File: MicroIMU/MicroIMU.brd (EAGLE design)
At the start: 8.1 x 9.3 mm, 17 parts

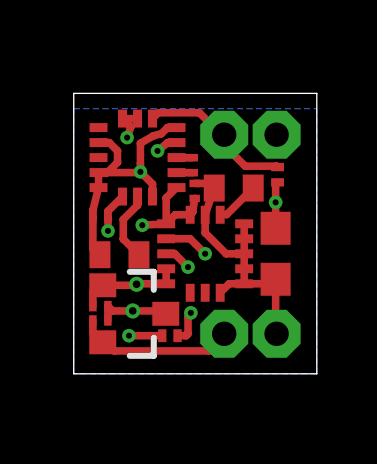
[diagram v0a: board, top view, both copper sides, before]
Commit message: changed to invense MPU9250
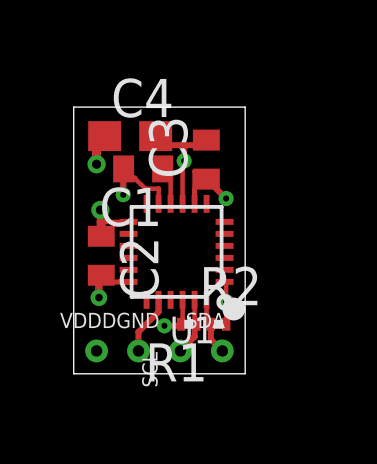
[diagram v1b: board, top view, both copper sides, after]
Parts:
- removed C5: 10uF, resistor:C0603
- removed C7: 0.01 uF, resistor:C0402
- removed C8: 4.7uF, resistor:C0402
- removed C9: 0.22 uF, resistor:C0201
- removed GND: GND, wirepad:1,6/0,8
- removed U$1: L3GD20H, st:LGA16L
- removed U$2: LM3480IM4, SparkFun-PowerIC:SOT23-3
- removed U$3: LSM303D, st:LGA16L
- removed VIN: 15V, wirepad:1,6/0,8
- added DGND, VDD: (no value), michael-stetner:30MIL/15MIL
- added U1: (no value), Grove - IMU 10DOF v1.1:LEAD-QFN24
- C1, C2: device resistor:C0201 -> resistor:C0402
- C3: value 0.1uF -> 10nF; device resistor:C0201 -> resistor:C0402
- C4: value 0.1uF -> 10uF; device resistor:C0201 -> resistor:C0603
- SCL: value SCL -> (none); device wirepad:1,6/0,8 -> michael-stetner:30MIL/15MIL
- SDA: value SDA -> (none); device wirepad:1,6/0,8 -> michael-stetner:30MIL/15MIL
- moved SCL 7.89 mm to (3.56, 0.76), turned to 90 degrees
- moved SDA 7.21 mm to (4.95, 0.76)
- moved R1 5.80 mm to (3.84, 1.65), turned to 180 degrees
- moved C1 5.25 mm to (2.31, 6.83), turned to 180 degrees
- moved C3 4.03 mm to (4.42, 7.14), turned to 90 degrees
- moved C4 2.82 mm to (1.88, 7.92), turned to 0 degrees
- moved C2 1.68 mm to (0.92, 3.94), turned to 270 degrees
- moved R2 1.66 mm to (4.83, 1.65), turned to 0 degrees
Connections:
- removed net +15V: C1.1, U$2.2, VIN.1
- removed net +3V3: C2.1, C3.1, C4.1, C5.1, R1.2, R2.2, U$1.P$1, U$1.P$16, U$1.P$4, U$1.P$5, U$2.1, U$3.P$1, U$3.P$14, U$3.P$7, U$3.P$8
- removed net GND: C1.2, C2.2, C3.2, C4.2, C5.2, C7.2, C8.2, GND.1, U$1.P$10, U$1.P$11, U$1.P$12, U$1.P$13, U$1.P$15, U$1.P$8, U$1.P$9, U$2.3, U$3.P$10, U$3.P$12, U$3.P$13, U$3.P$16, U$3.P$5
- removed net N$1: C8.1, U$3.P$15
- removed net N$2: C9.1, U$3.P$3
- removed net N$3: C9.2, U$3.P$2
- removed net N$9: C7.1, U$1.P$14
- new net DGND: C1.2, C2.2, C3.2, C4.2, DGND.P$1, U1.11, U1.18, U1.20, U1.9
- new net N$7: C1.1, U1.10
- new net VDD: C2.1, C3.1, C4.1, R1.2, R2.2, U1.1, U1.13, U1.22, U1.8, VDD.P$1
- net SCL: now also R1.1, SCL.P$1, U1.23; no longer R2.1, SCL.1, U$1.P$2, U$3.P$4
- net SDA: now also R2.1, SDA.P$1, U1.24; no longer R1.1, SDA.1, U$1.P$3, U$3.P$6
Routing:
- net GND: track 22.3 -> 0.00 mm, vias 2 -> 0
- net SCL: track 17.0 -> 1.98 mm, vias 3 -> 0
- net +3V3: track 13.7 -> 0.00 mm, vias 6 -> 0
- net DGND: track 0.00 -> 11.8 mm, vias 0 -> 3
- net VDD: track 0.00 -> 10.6 mm, vias 0 -> 5
- net SDA: track 11.0 -> 1.99 mm, vias 1 -> 0
- net +15V: track 5.27 -> 0.00 mm
- net N$1: track 2.35 -> 0.00 mm
- net N$9: track 1.49 -> 0.00 mm
- net N$7: track 0.00 -> 1.41 mm
- net N$3: track 0.54 -> 0.00 mm
- net N$2: track 0.54 -> 0.00 mm
- added copper zone on layer 2, net DGND
- added copper zone on layer 15, net VDD
- removed copper zone on layer 2, net +3V3
- removed copper zone on layer 16, net GND
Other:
- board size 8.1 x 9.3 mm -> 5.7 x 8.9 mm
- board text added: "GND"
- board text added: "MicroIMU"
- board text added: "SCL"
- board text added: "SDA"
- board text added: "VDD"
- board text added: "X"
- board text added: "Y"
- board text added: "Z"
